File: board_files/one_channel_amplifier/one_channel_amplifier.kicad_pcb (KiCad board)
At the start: 2 copper layers, 50.8 x 50.8 mm, 27 parts, among them J1 Screw_Terminal_01x02, J2 Screw_Terminal_01x02, J3 Screw_Terminal_01x02, J4 Conn_01x02, J5 Conn_01x02, J6 Screw_Terminal_01x02, U1 LM3886

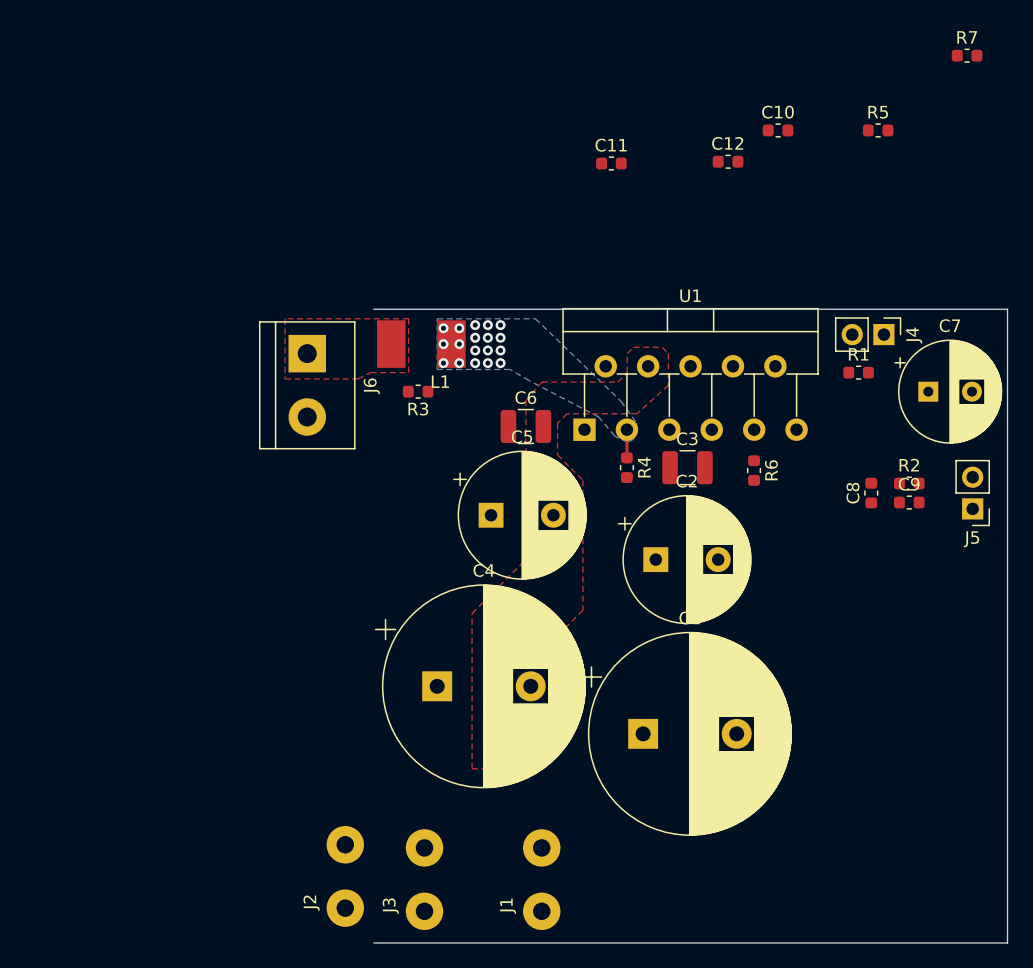
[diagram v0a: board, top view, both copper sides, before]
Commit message: removed other PCB designs
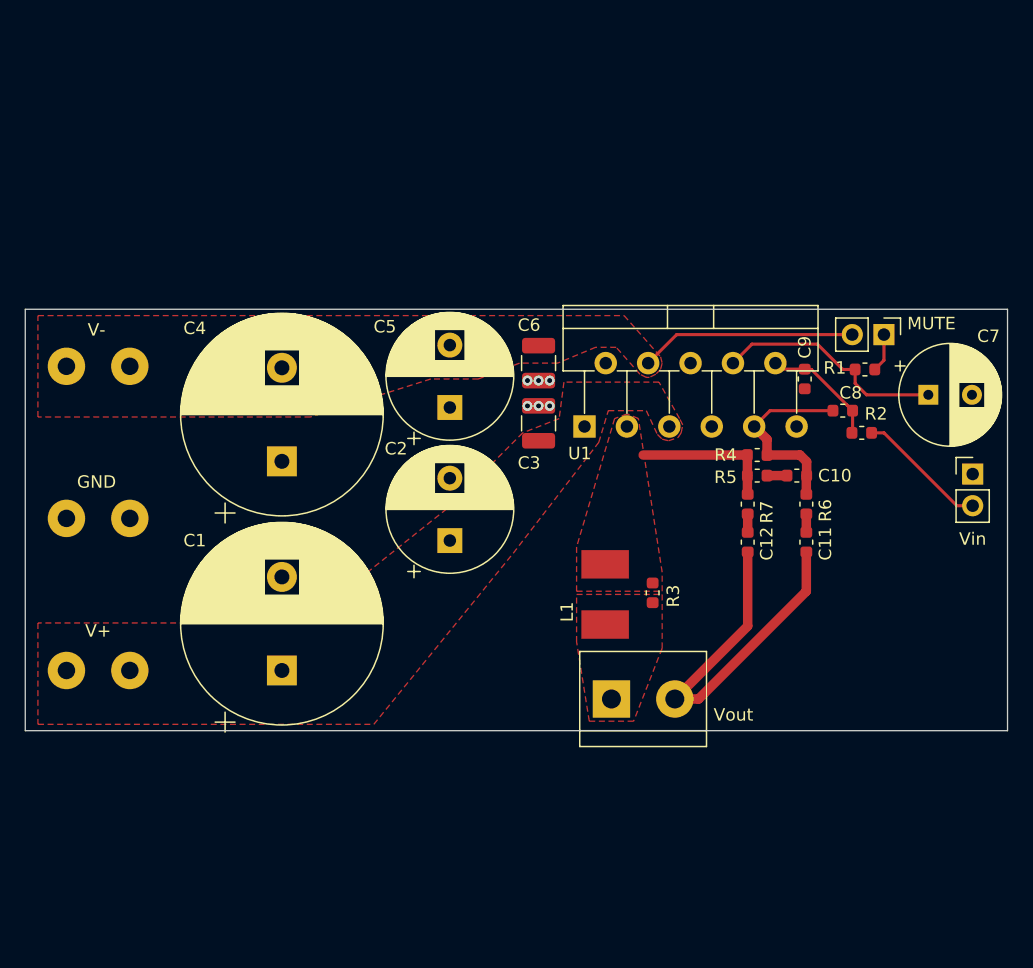
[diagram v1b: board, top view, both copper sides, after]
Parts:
- moved J3 49.7 mm to (107.4, 80.8), turned to 180 degrees
- moved R7 40.0 mm to (157.0, 91.8), turned to 270 degrees
- moved J1 38.2 mm to (107.4, 105.2), turned to 180 degrees
- moved J6 36.9 mm to (146.1, 107.4), turned to 0 degrees
- moved J2 35.7 mm to (107.4, 93.0), turned to 180 degrees
- moved C11 34.1 mm to (161.7, 94.9), turned to 270 degrees
- moved C12 30.5 mm to (157.0, 94.9), turned to 270 degrees
- moved C1 29.4 mm to (119.6, 105.2), turned to 90 degrees
- moved R5 29.3 mm to (157.7, 89.5)
- moved C10 27.7 mm to (160.9, 89.5), turned to 180 degrees
- moved L1 24.9 mm to (145.5, 99.1), turned to 270 degrees
- moved R3 24.8 mm to (149.4, 98.9), turned to 270 degrees
- moved C4 21.9 mm to (119.6, 88.4), turned to 90 degrees
- moved C2 16.6 mm to (133.1, 94.7), turned to 90 degrees
- moved C9 13.0 mm to (161.5, 81.8), turned to 270 degrees
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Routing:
- net GND: track 0.00 -> 31.5 mm, vias 0 -> 6
- net Net-(C7-Pad1): track 0.00 -> 18.6 mm
- net VEE: track 0.00 -> 17.3 mm
- net Net-(C10-Pad1): track 0.00 -> 15.6 mm
- net Net-(J5-Pad2): track 0.00 -> 10.5 mm
- net Net-(C8-Pad2): track 0.00 -> 9.57 mm
- net Net-(L1-Pad1): track 2.26 -> 11.5 mm, vias 18 -> 0
- net Net-(J4-Pad1): track 0.00 -> 3.10 mm
- net Net-(C10-Pad2): track 0.00 -> 1.60 mm
- net Net-(C12-Pad1): track 0.00 -> 1.47 mm
- net Net-(C11-Pad1): track 0.00 -> 1.47 mm
- added copper zone on F.Cu, net Net-(L1-Pad1)
- added copper zone on F.Cu, net VCC
- removed copper zone on B.Cu, net Net-(L1-Pad1)
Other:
- board size 50.8 x 50.8 mm -> 78.7 x 33.8 mm
- board text added: "GND"
- board text added: "MUTE"
- board text added: "V+"
- board text added: "V-"
- board text added: "Vin"
- board text added: "Vout"
